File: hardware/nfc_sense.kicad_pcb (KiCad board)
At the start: 2 copper layers, 18.6 x 44.5 mm, 22 parts, among them U1 TMP112AIDRLT, U2 RF430CL330HIRGTR‎, U3 ATtiny3227-M

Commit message: attiny426 revision
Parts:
- added VCC: TestPoint, TestPoint:TestPoint_Pad_D1.0mm, B.Cu at (133.9, 42.5)
- U3: value ATtiny3227-M -> ATtiny426-M; footprint Package_DFN_QFN:QFN-24-1EP_4x4mm_P0.5mm_EP2.6x2.6mm -> Package_DFN_QFN:VQFN-20-1EP_3x3mm_P0.4mm_EP1.7x1.7mm
- moved R1 1.06 mm to (127.2, 45.7)
- moved U3 0.56 mm to (127.3, 50.0)
- moved C2 0.30 mm to (129.1, 55.4)
- moved C7 0.20 mm to (125.9, 55.4)
- renumbered TP4 to GND, GND1 to GND, TP1 to RX, TP2 to TX, UPDI1 to UPDI, VCC1 to VCC
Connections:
- U3 pad 11: unconnected-(U3-Pad11) -> RX
- U3 pad 12: RST -> TX
- U3 pad 13: RX -> SDA
- U3 pad 14: TX -> SCL
- U3 pad 15: SDA -> unconnected-(U3-Pad15)
- U3 pad 16: SCL -> unconnected-(U3-Pad16)
- U3 pad 18: unconnected-(U3-Pad18) -> ALERT
- U3 pad 19: unconnected-(U3-Pad19) -> UPDI
- U3 pad 21: unconnected-(U3-Pad21) -> GND
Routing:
- net VCC: track 48.0 -> 54.6 mm, vias 7 -> 8
- net UPDI: track 7.32 -> 8.59 mm
- net GND: track 56.2 -> 55.1 mm
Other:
- board size 18.6 x 44.5 mm -> 18.6 x 43.1 mm

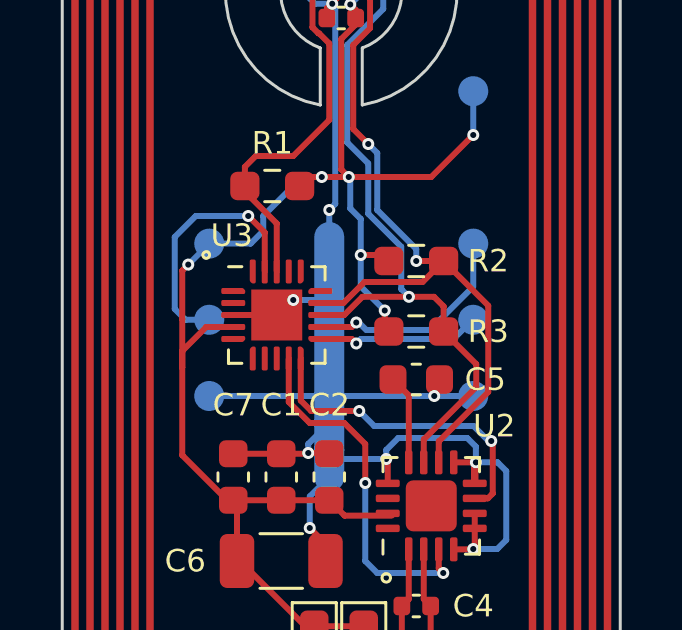
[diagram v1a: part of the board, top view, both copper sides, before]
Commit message: changed to attiny 1626
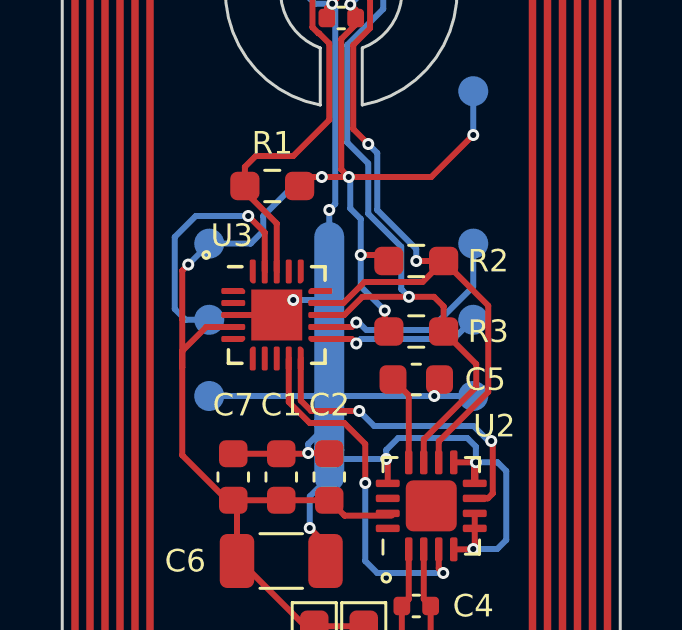
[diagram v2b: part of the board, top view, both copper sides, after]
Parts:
- C1: value 1 yF -> 1 uF
- C2, C3, C7: value 0.1 yF -> 0.1 uF
- C5: value 0.47 yF -> 0.47 uF
- D1, D2: value D_Schottky -> CDBU0130L
- U1: value TMP112AIDRLT -> TMP117AIYBGR
- U3: value ATtiny426-M -> ATtiny1626-MFR
- renumbered GND to GND1, RX to TP1, TX to TP2, GND to TP3, VCC to TP4, UPDI to UPDI1, VCC to VCC1

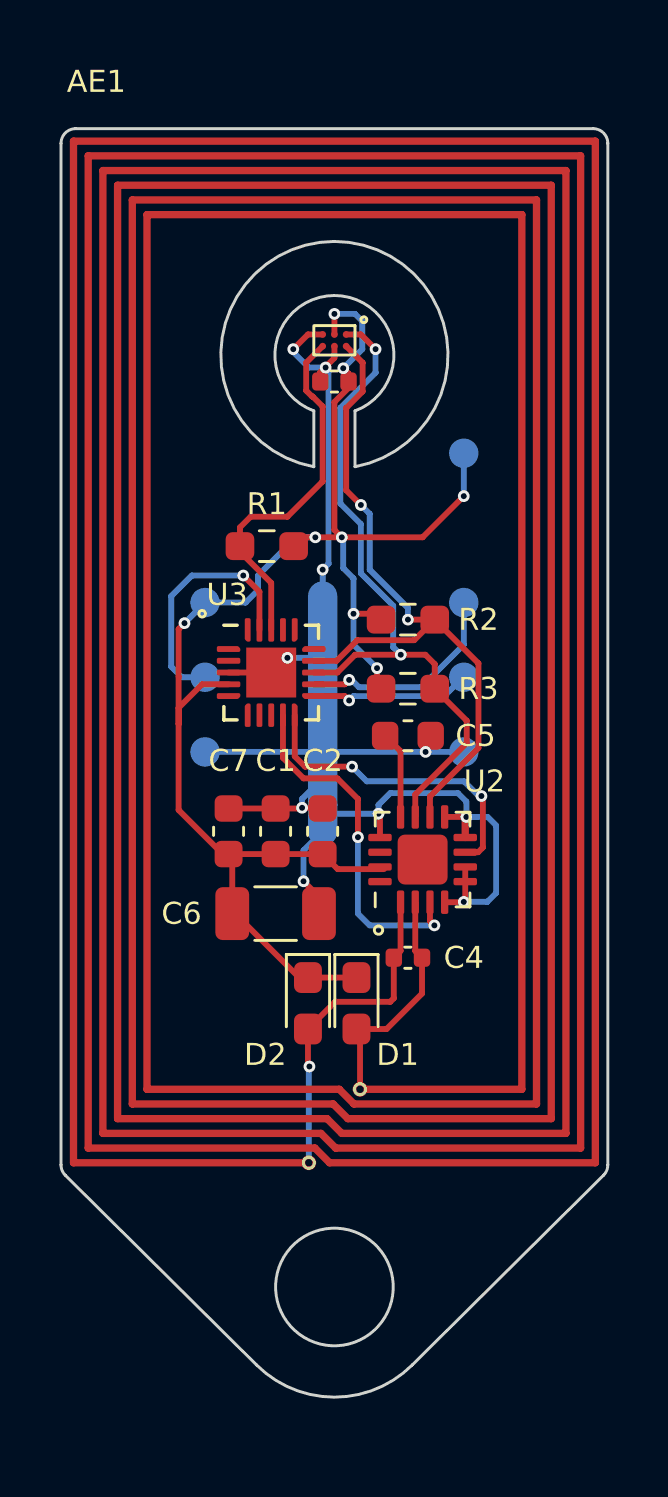
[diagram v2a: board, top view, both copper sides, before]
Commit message: individual case part cutouts
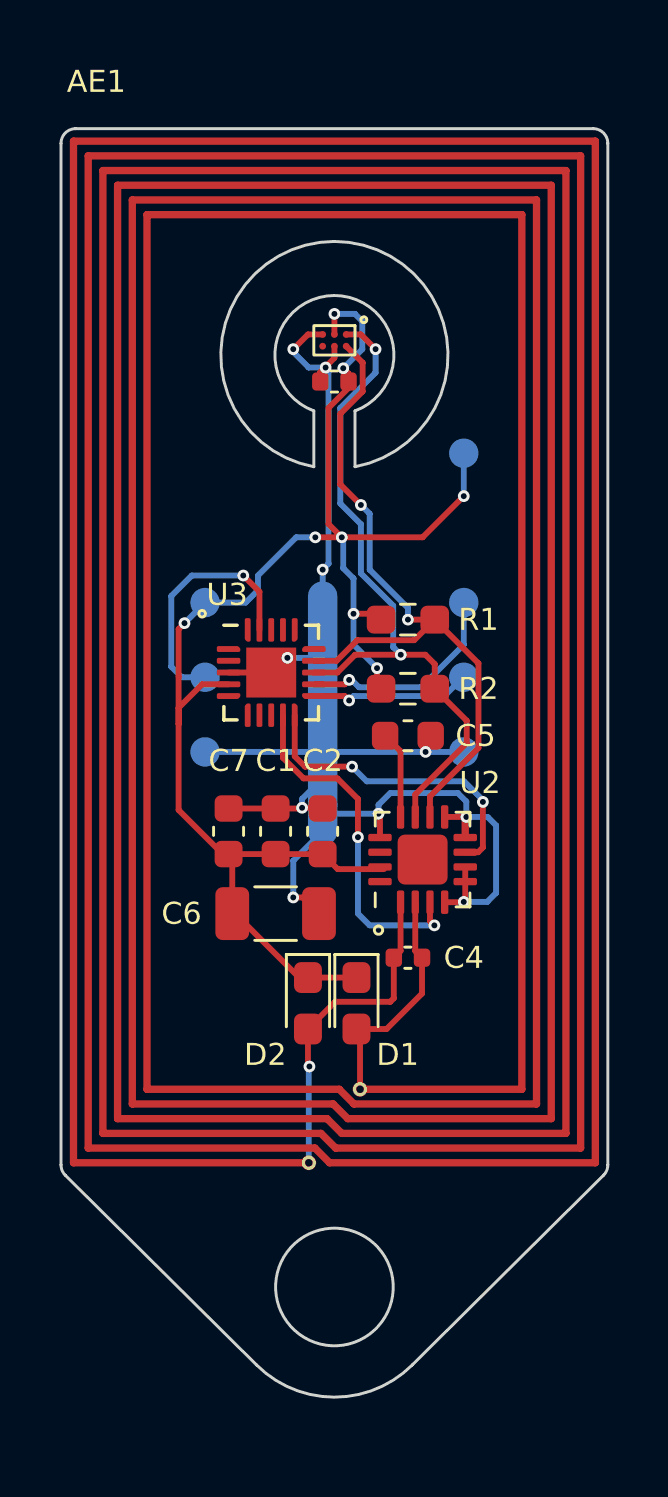
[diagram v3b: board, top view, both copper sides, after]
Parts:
- removed the R1 at (127.2, 45.7)
- added QR_ref1: TestPoint, unsurv_offline_pcb_footprints:QR_shop, B.Cu at (129.5, 58.7)
- renumbered R2 to R1, R3 to R2
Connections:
- U1 pad 3: ALERT -> unconnected-(U1-Pad3)
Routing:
- net ALERT: track 12.5 -> 0.00 mm
- net VCC: track 54.6 -> 53.9 mm
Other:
- board text added: "VCC TX RX GND"
- board text added: "VCC UPDI GND"
- board text added: "v 0.8 pre-production 03/24"

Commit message: rev 2
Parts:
- added C7: 47uF, Capacitor_SMD:C_0603_1608Metric, F.Cu at (127.5, 59.2)
- C6: value 100uF -> 47uF; footprint Capacitor_SMD:C_1206_3216Metric -> Capacitor_SMD:C_0603_1608Metric
- U1: value TMP117AIYBGR -> TMP117AIDRVR; footprint unsurv_offline_pcb_footprints:TMP117 -> unsurv_offline_pcb_footprints:TMP117 WSON-6-1EP_2x2mm_P0.65mm
- moved C3 0.55 mm to (129.5, 40.6)
- moved D2 0.51 mm to (128.7, 61.8)
- moved D1 0.50 mm to (130.3, 61.8)
- moved C6 0.50 mm to (127.5, 57.7)
- moved C5 0.30 mm to (132.0, 52.5)
- renumbered C7 to C8
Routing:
- net GND: track 55.6 -> 62.0 mm
- net SCL: track 24.4 -> 26.6 mm
- net VCC: track 53.9 -> 51.8 mm, vias 8 -> 6
- net SDA: track 23.8 -> 22.8 mm
- net UPDI: track 8.59 -> 8.02 mm
- net ANT1: track 11.5 -> 10.9 mm
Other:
- outline, holes or cut-outs redrawn
- board text added: "v 0.9 pre-production 09/24"
- board text removed: "v 0.8 pre-production 03/24"

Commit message: kicad 8 + panelization
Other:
- copper layers 2 -> 4

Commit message: desc + new TP
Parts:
- added TP5: TestPoint, TestPoint:TestPoint_Pad_D1.0mm, B.Cu at (133.9, 60.9)
- U1: footprint unsurv_offline_pcb_footprints:TMP117 WSON-6-1EP_2x2mm_P0.65mm -> unsurv_offline_pcb_footprints:TMP117 WSON-6-1EP_2x2mm_P0.65mm_no_pad_paste
- moved TP4 2.54 mm to (133.9, 45.1)
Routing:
- net VCC: track 51.8 -> 50.2 mm
- net ANT2: track 7.67 -> 9.10 mm, vias 0 -> 1
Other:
- board text added: "VCC TX RX GND NFC"
- board text added: "v 1.0 Made in Germany 11/24"
- board text removed: "VCC TX RX GND"
- board text removed: "v 0.9 pre-production 09/24"

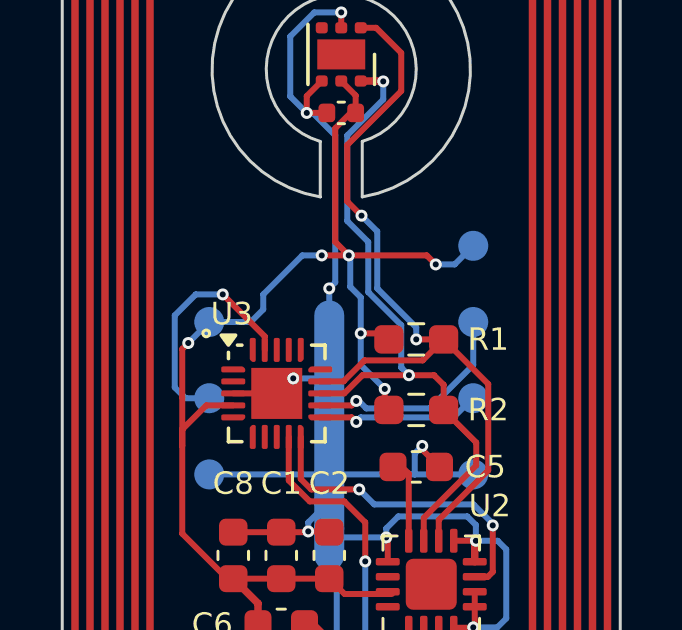
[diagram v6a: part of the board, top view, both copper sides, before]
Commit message: new panel frame
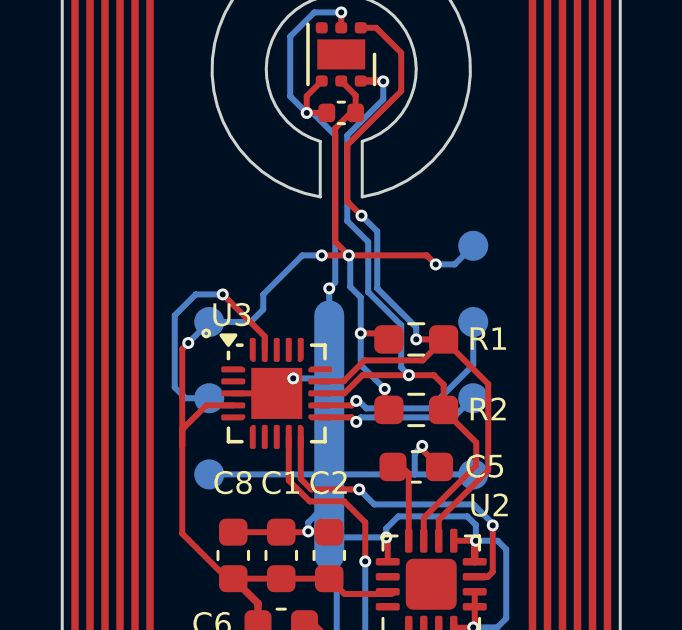
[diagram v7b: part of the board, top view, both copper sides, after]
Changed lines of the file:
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@@
 		(tags "VQFN NoLead")
 		(property "Reference" "U3"
-			(at -1.5 -2.65 0)
+			(at -1.5 -2.6 0)
 			(unlocked yes)
 			(layer "F.SilkS")

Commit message: update labeling
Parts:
- C6: value 47uF -> 100uF
- C7: value 47uF -> 1uf
- D1, D2: footprint Diode_SMD:D_0603_1608Metric_Pad1.05x0.95mm_HandSolder -> Diode_SMD:D_0603_1608Metric
- R1, R2: footprint Resistor_SMD:R_0603_1608Metric_Pad0.98x0.95mm_HandSolder -> Resistor_SMD:R_0603_1608Metric
- U2: footprint unsurv_offline_pcb_footprints:RF430_3x3mm_noBCu -> unsurv_offline_pcb_footprints:RF430_3x3mm_regular
- U3: footprint Package_DFN_QFN:VQFN-20-1EP_3x3mm_P0.4mm_EP1.7x1.7mm -> unsurv_offline_pcb_footprints:VQFN-20-1EP_3x3mm_P0.4mm_EP1.7x1.7mm_edited
